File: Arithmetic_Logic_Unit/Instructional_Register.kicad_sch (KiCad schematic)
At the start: 2 parts, among them IC1 SN54173J, IC2 SN54173J

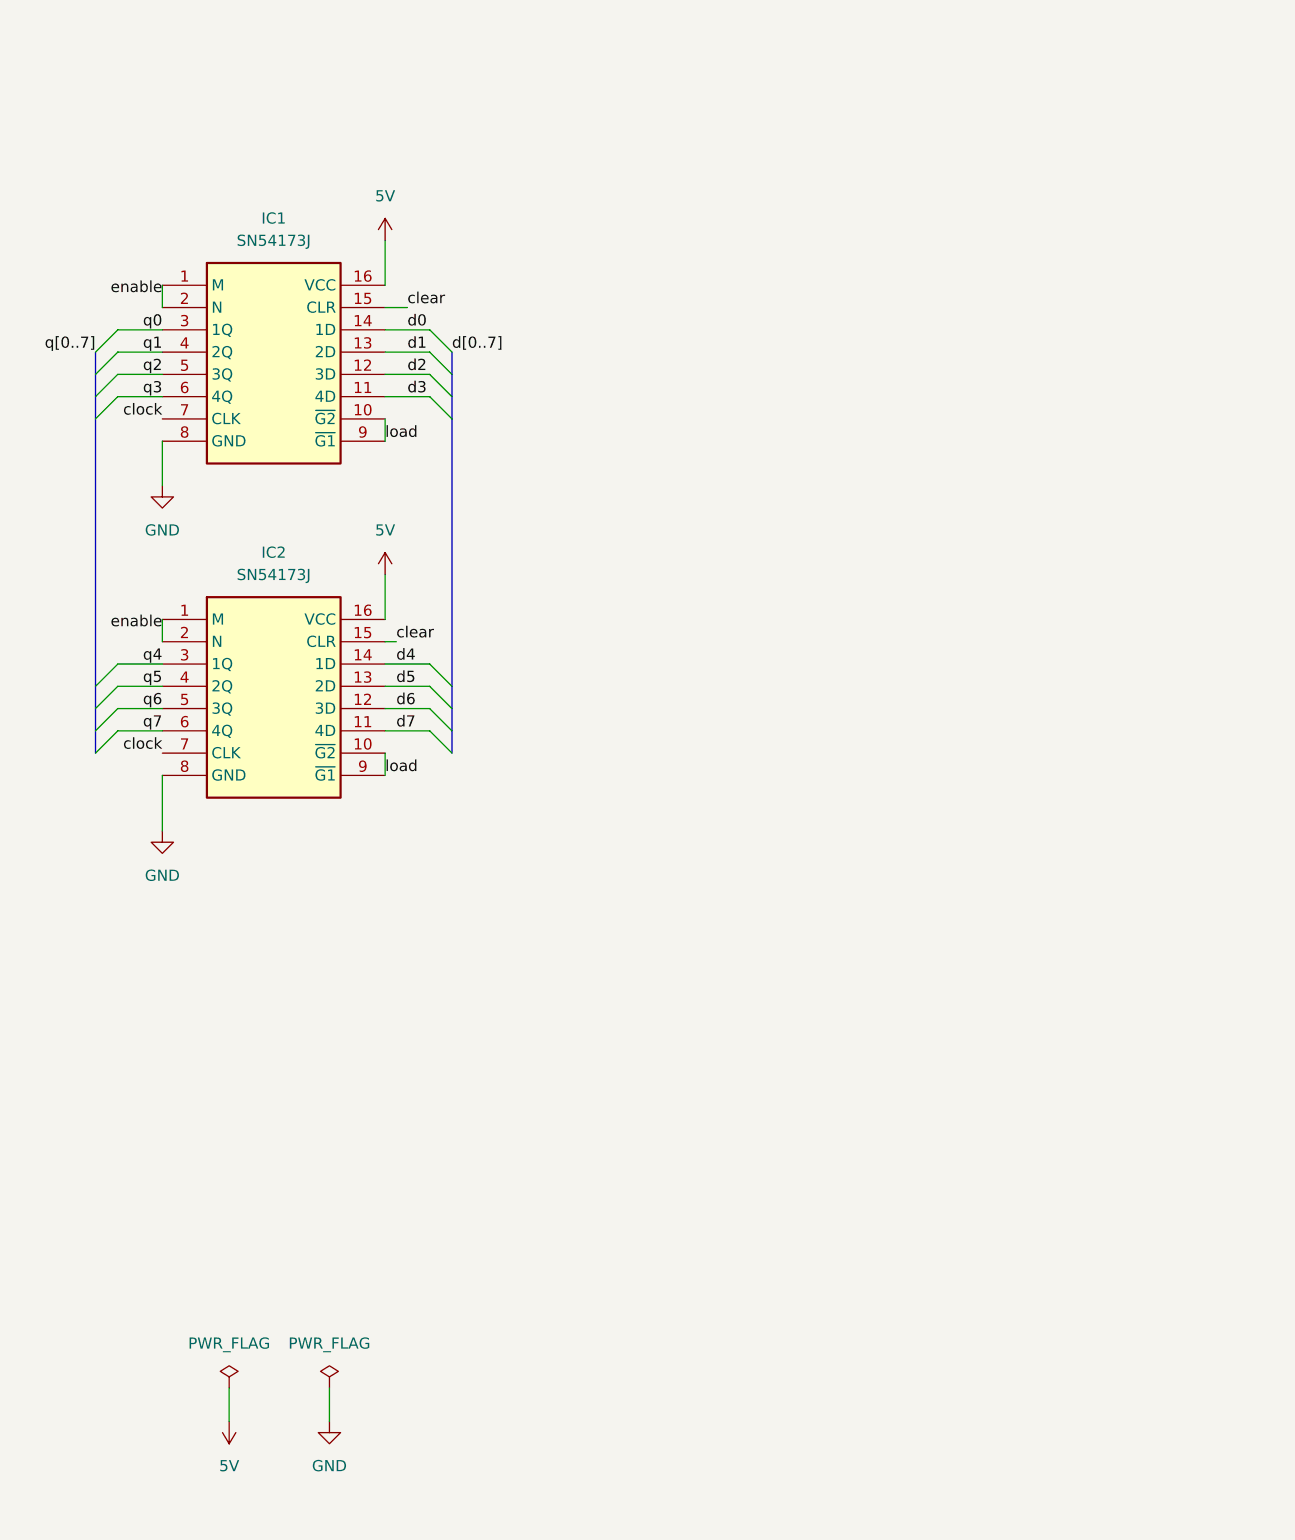
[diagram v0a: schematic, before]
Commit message: added A, B, and Instructional Regsiters
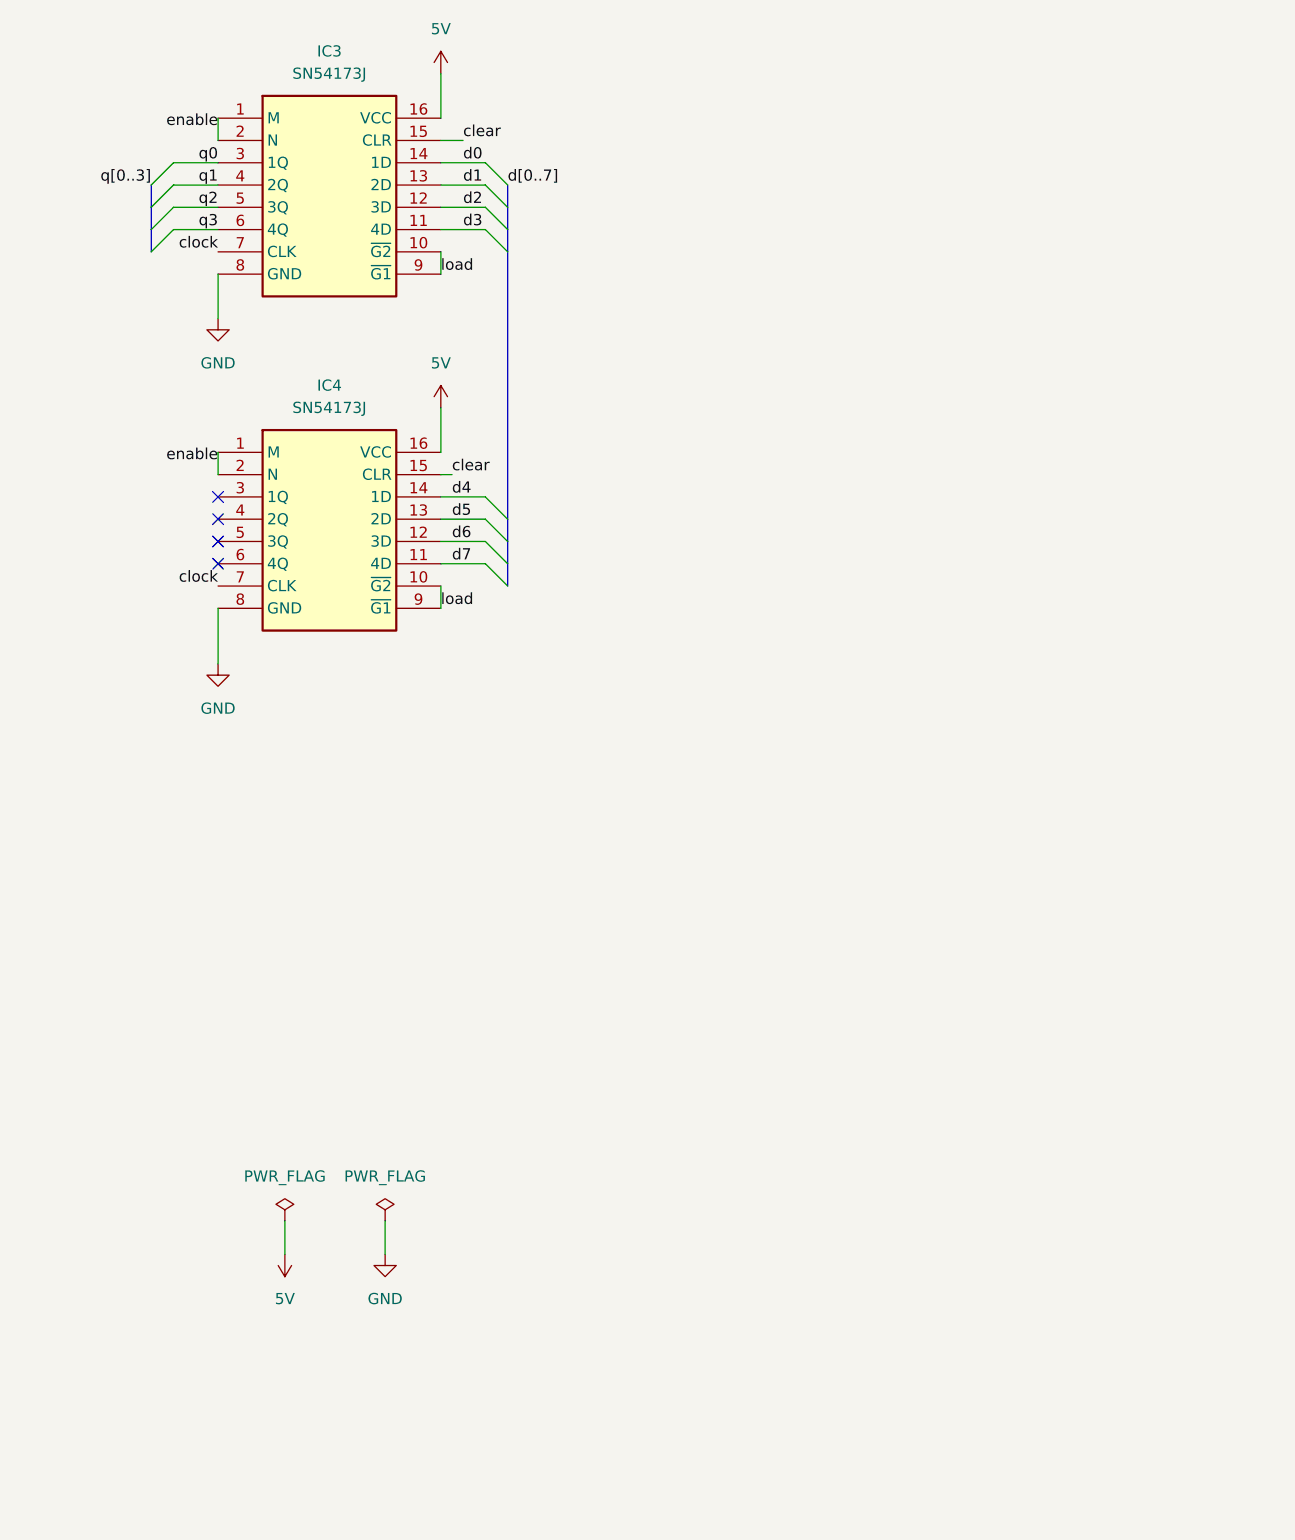
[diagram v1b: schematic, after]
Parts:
- removed IC1, IC2: SN54173J, CDIP762W66P254L2134H508Q16, symbol SN54173J:SN54173J
- added IC3, IC4: SN54173J, CDIP762W66P254L2134H508Q16, symbol SN54173J:SN54173J
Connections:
- net 5V: now also IC3.16 (VCC), IC4.16 (VCC)
- net GND: now also IC3.8 (GND), IC4.8 (GND)
- net clear: now also IC3.15 (CLR), IC4.15 (CLR)
- net clock: now also IC3.7 (CLK), IC4.7 (CLK)
- net d0: now also IC3.14 (1D)
- net d1: now also IC3.13 (2D)
- net d2: now also IC3.12 (3D)
- net d3: now also IC3.11 (4D)
- net d4: now also IC4.14 (1D)
- net d5: now also IC4.13 (2D)
- net d6: now also IC4.12 (3D)
- net d7: now also IC4.11 (4D)
- net enable: now also IC3.1 (M), IC3.2 (N), IC4.1 (M), IC4.2 (N)
- net load: now also IC3.10 (~{G2}), IC3.9 (~{G1}), IC4.10 (~{G2}), IC4.9 (~{G1})
- net q0: now also IC3.3 (1Q)
- net q1: now also IC3.4 (2Q)
- net q2: now also IC3.5 (3Q)
- net q3: now also IC3.6 (4Q)
- no-connect marks 0 -> 4
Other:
- title: Registers -> Instructional Register

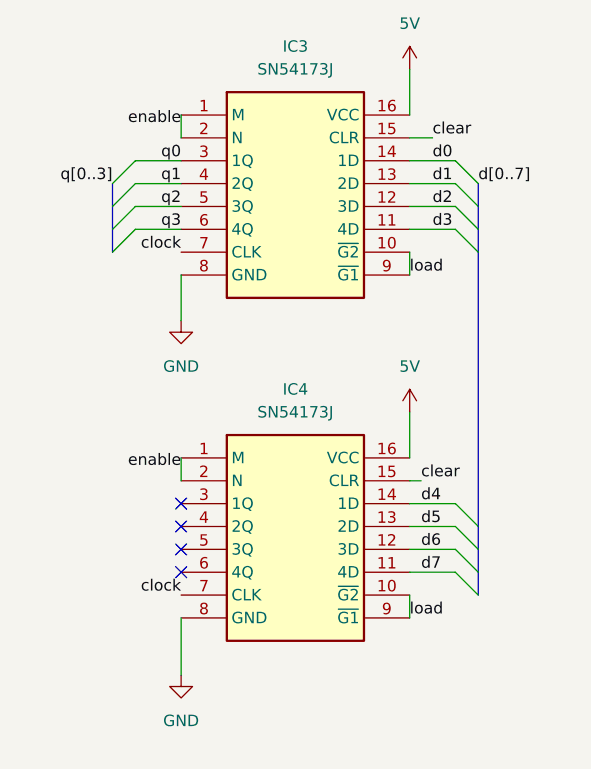
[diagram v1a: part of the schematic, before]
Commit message: updated wiki, created board outline for alu, made registers with hierarchical label
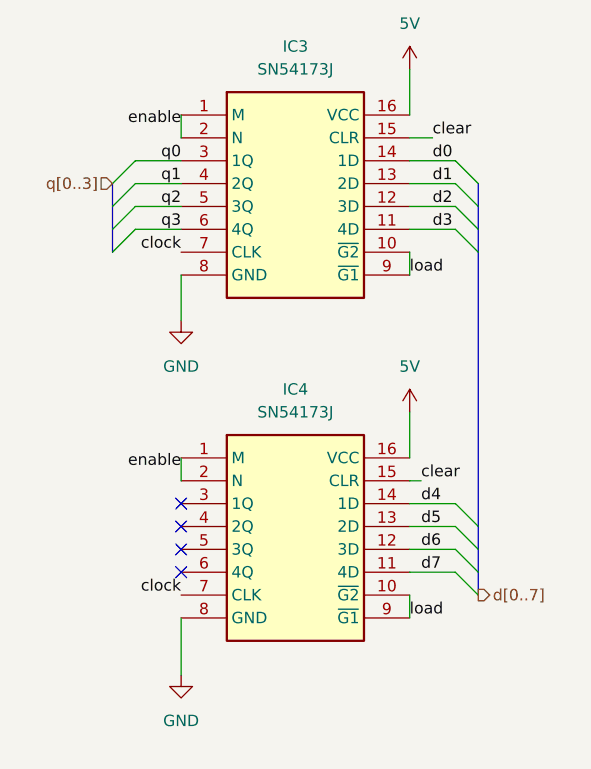
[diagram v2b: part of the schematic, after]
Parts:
- IC3, IC4: footprint CDIP762W66P254L2134H508Q16 -> footprints:SN54173J
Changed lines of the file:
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@@
-		)
-	)
-	(label "q[0..3]"
-		(at 40.64 44.45 180)
-		(fields_autoplaced yes)
-		(effects
-			(font
-				(size 1.27 1.27)
-			)
-			(justify right bottom)
 		)
 	)
@@
 		)
 	)
-	(label "d[0..7]"
-		(at 81.28 44.45 0)
-		(fields_autoplaced yes)
-		(effects
-			(font
-				(size 1.27 1.27)
-			)
-			(justify left bottom)
-		)
-	)
 	(label "d6"
 		(at 74.93 85.09 0)
@@
 		)
 	)
+	(hierarchical_label "d[0..7]"
+		(shape output)
+		(at 81.28 90.17 0)
+		(fields_autoplaced yes)
+		(effects
+			(font
+				(size 1.27 1.27)
+			)
+			(justify left)
+		)
+	)
+	(hierarchical_label "q[0..3]"
+		(shape input)
+		(at 40.64 44.45 180)
+		(fields_autoplaced yes)
+		(effects
+			(font
+				(size 1.27 1.27)
+			)
+			(justify right)
+		)
+	)
 	(symbol
 		(lib_id "SN54173J:SN54173J")
@@
 			)
 		)
-		(property "Footprint" "CDIP762W66P254L2134H508Q16"
+		(property "Footprint" "footprints:SN54173J"
 			(at 69.85 169.85 0)
 			(effects
@@
 			)
 		)
-		(property "Footprint" "CDIP762W66P254L2134H508Q16"
+		(property "Footprint" "footprints:SN54173J"
 			(at 69.85 131.75 0)
 			(effects

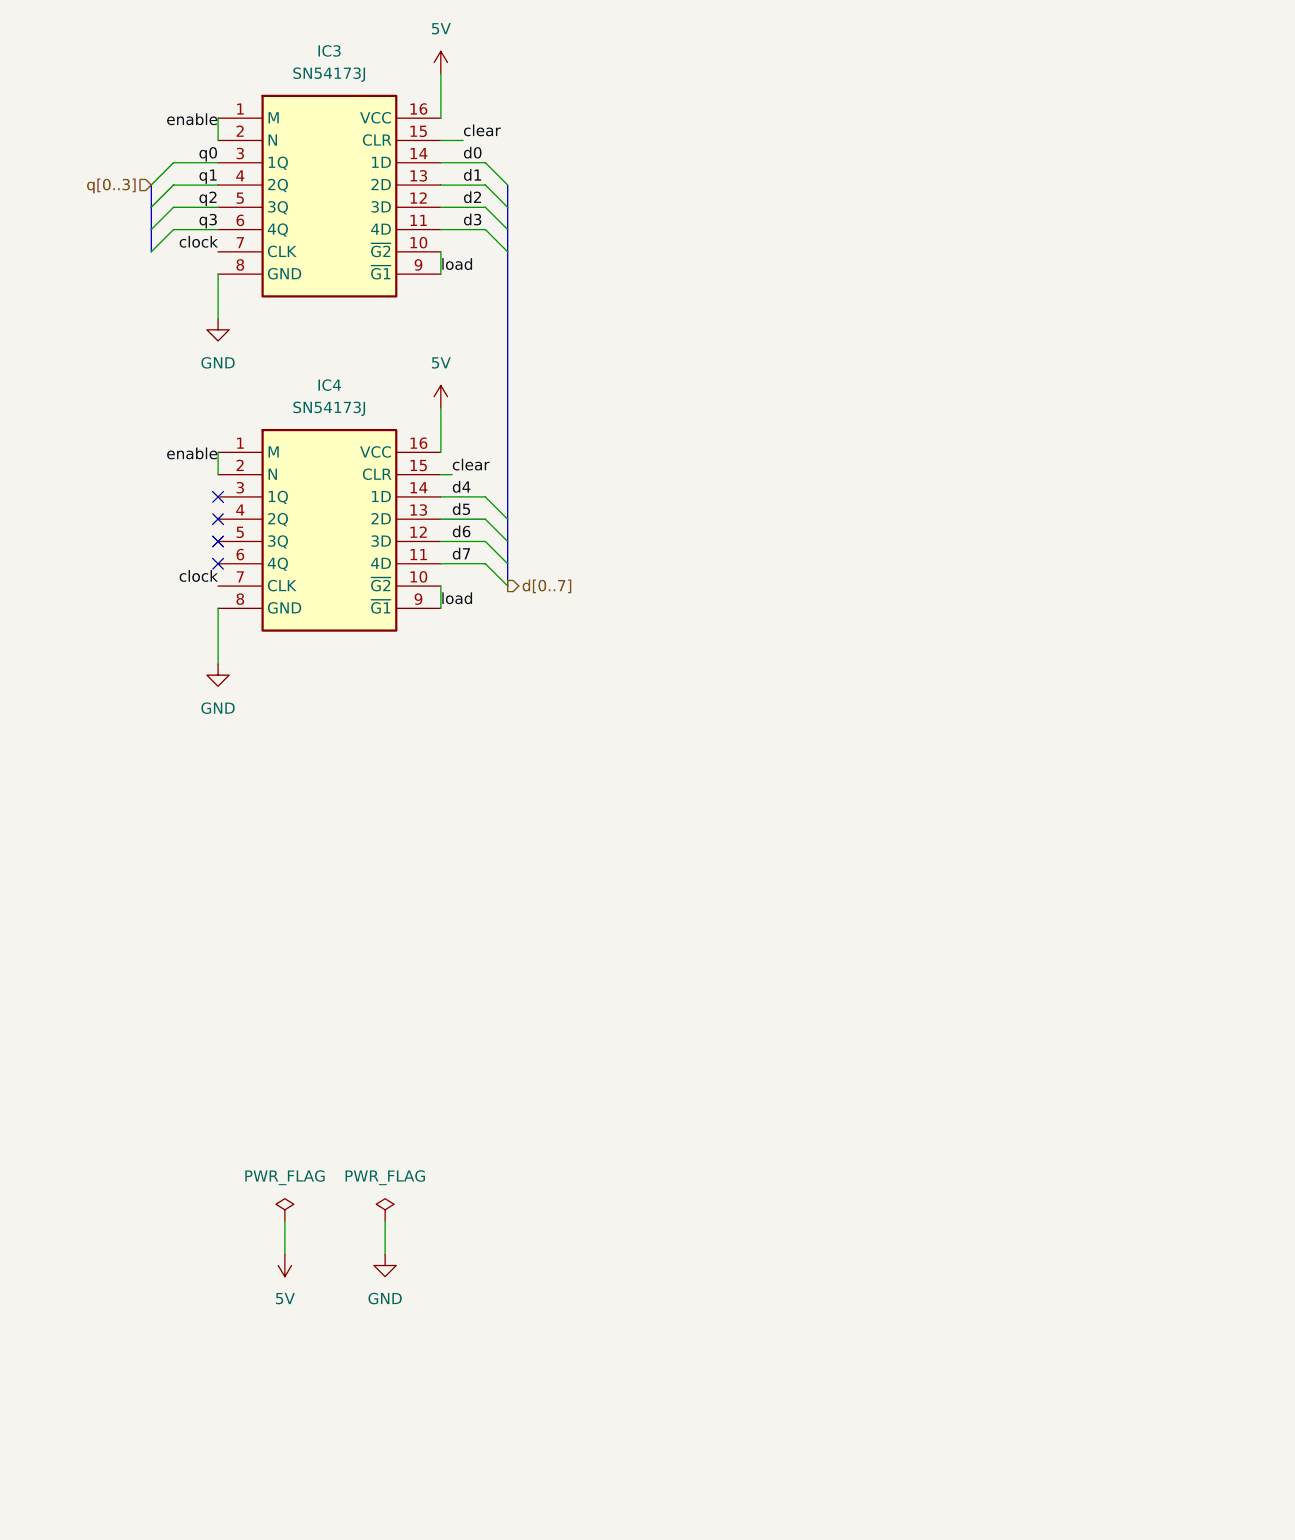
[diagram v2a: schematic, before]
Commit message: fixed register schematic
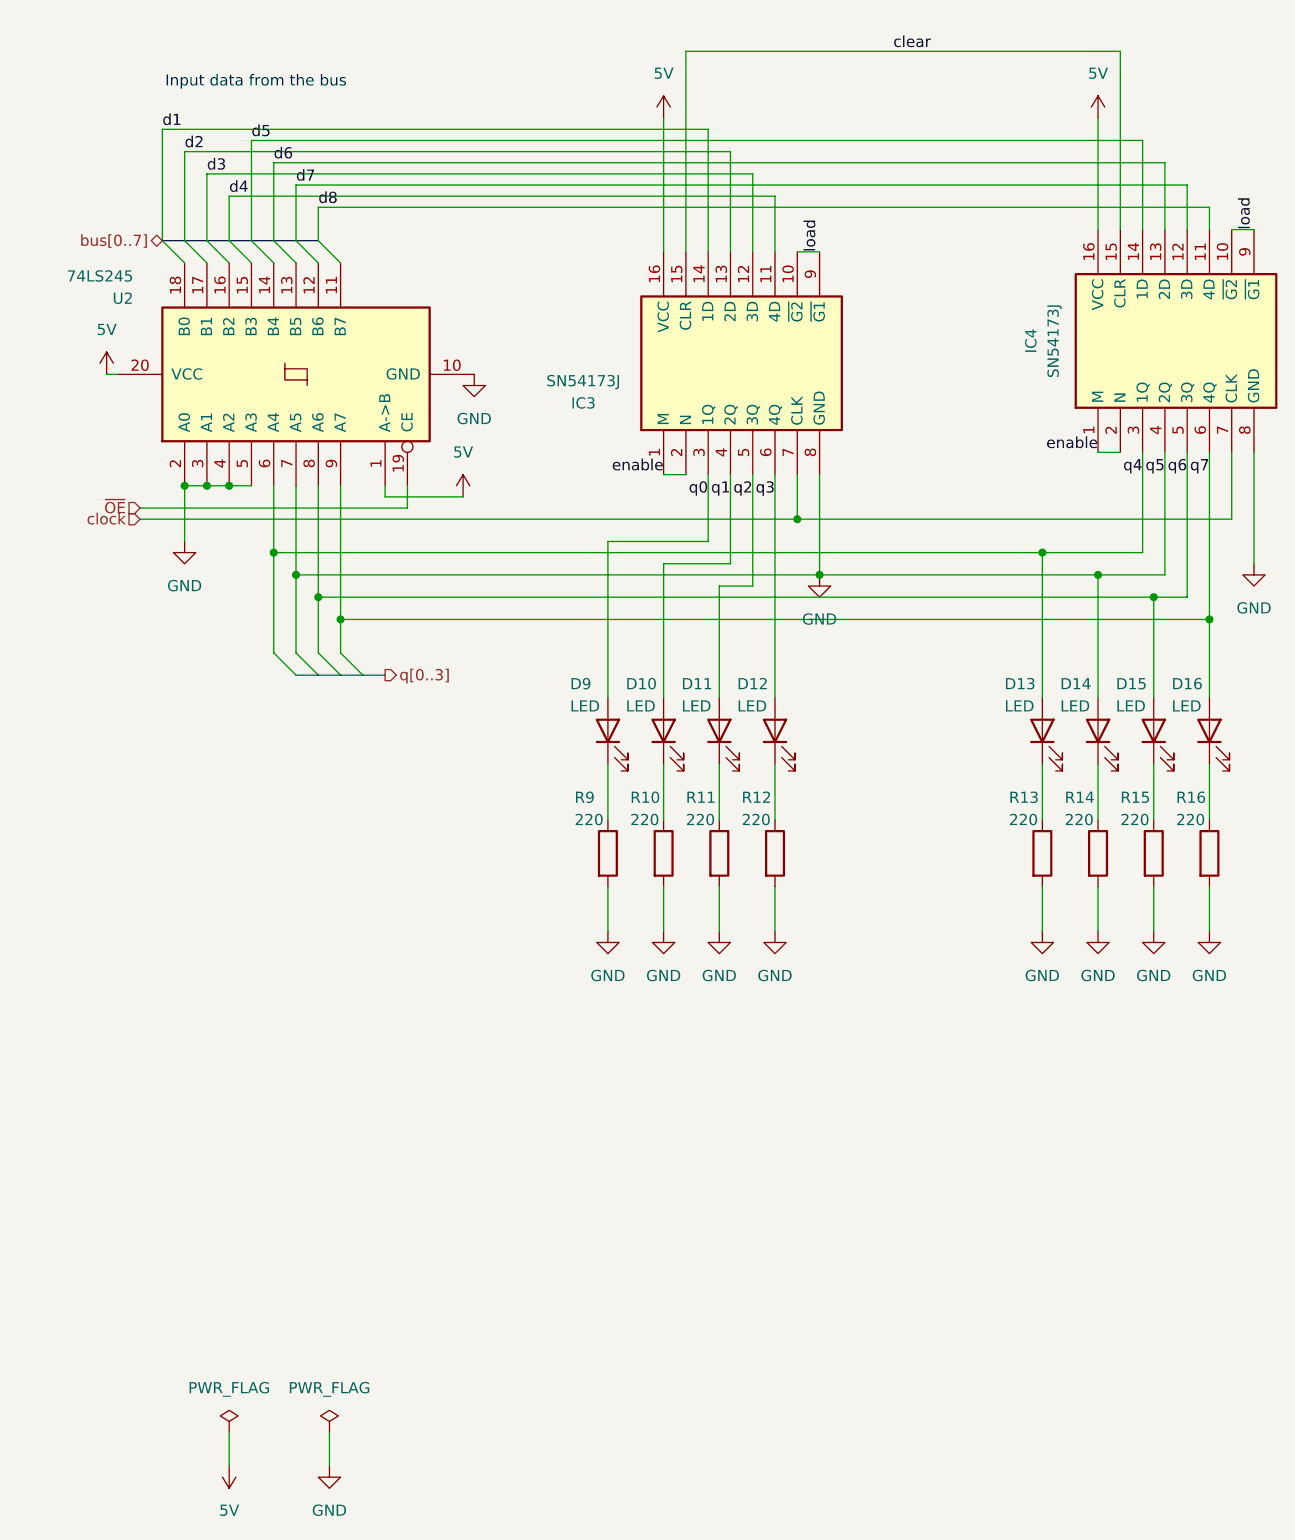
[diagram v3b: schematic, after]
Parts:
- added D10, D11, D12, D13, D14, D15, D16, D9: LED, symbol Device:LED
- added R10, R11, R12, R13, R14, R15, R16, R9: 220, symbol Device:R
- added U2: 74LS245, symbol 74xx:74LS245
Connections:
- net d1 is gone; now on net d2: IC3.13 (2D)
- net 5V: now also U2.1 (A->B), U2.20 (VCC)
- net GND: now also IC4.4 (2Q), D14.2 (A), R10.2, R11.2, R12.2, R13.2, R14.2, R15.2, R16.2, R9.2, U2.10 (GND), U2.2 (A0), U2.3 (A1), U2.4 (A2), U2.5 (A3), U2.7 (A5)
- net d2: no longer IC3.12 (3D)
- net d3: now also IC3.12 (3D); no longer IC3.11 (4D)
- net d4: now also IC3.11 (4D); no longer IC4.14 (1D)
- net d5: now also IC4.14 (1D); no longer IC4.13 (2D)
- net d6: now also IC4.13 (2D); no longer IC4.12 (3D)
- net d7: now also IC4.12 (3D); no longer IC4.11 (4D)
- net q0: now also D9.2 (A)
- net q1: now also D10.2 (A)
- net q2: now also D11.2 (A)
- net q3: now also D12.2 (A)
- net q4: now reaches IC4.3 (1Q)
- net q4: now also D13.2 (A), U2.6 (A4)
- net q6: now reaches IC4.5 (3Q)
- net q6: now also D15.2 (A), U2.8 (A6)
- net q7: now reaches IC4.6 (4Q)
- net q7: now also D16.2 (A), U2.9 (A7)
- net d0 renamed bus[0..7]
- new net: D16.1 (K), R16.1
- new net: D11.1 (K), R11.1
- new net: D9.1 (K), R9.1
- new net: D15.1 (K), R15.1
- new net: D12.1 (K), R12.1
- new net: D14.1 (K), R14.1
- new net: D10.1 (K), R10.1
- new net: D13.1 (K), R13.1
- new net d8: IC4.11 (4D)
- new net ~{OE}: U2.19 (CE)
- no-connect marks 4 -> 0
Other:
- note added: "Input data from the bus"
